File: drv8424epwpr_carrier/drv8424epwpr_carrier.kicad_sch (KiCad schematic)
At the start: 27 parts, among them J1 Input_01x08, J2 Output_01x08, J3 POW_01x02, U1 DRV8424EPWPR, U2 DMP4013LFG-7

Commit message: get ready for PCB
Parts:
- U1: footprint DRV8424EPWPR:HTSSOP28_PWP_TEX -> DRV8424EPWPR:HTSSOP28_PWP_TEX-M
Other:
- note added: "3V3 GND nFAULT nSLEEP AEN APH BEN BPH"
- note added: "AOUT1 AOUT2 VREFA VM GND VREFB BOUT2 BOUT1"
- note added: "VIN GND"
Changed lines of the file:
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@@
+		)
+	)
+	(text "VIN\nGND"
+		(exclude_from_sim no)
+		(at 246.38 45.72 0)
+		(effects
+			(font
+				(size 1.524 1.524)
+			)
+		)
+	)
+	(text "3V3\nGND\nnFAULT\nnSLEEP\nAEN\nAPH\nBEN\nBPH"
+		(exclude_from_sim no)
+		(at 167.132 54.864 0)
+		(effects
+			(font
+				(size 1.524 1.524)
+			)
+		)
+	)
+	(text "AOUT1\nAOUT2\nVREFA\nVM\nGND\nVREFB\nBOUT2\nBOUT1"
+		(exclude_from_sim no)
+		(at 206.502 54.864 0)
+		(effects
+			(font
+				(size 1.524 1.524)
+			)
 		)
 	)
@@
 			)
 		)
-		(property "Footprint" "DRV8424EPWPR:HTSSOP28_PWP_TEX"
+		(property "Footprint" "DRV8424EPWPR:HTSSOP28_PWP_TEX-M"
 			(at 127 100.33 0)
 			(effects

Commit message: update layout
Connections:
- net +3V3: now also J1.8 (Pin_8); no longer J1.1 (Pin_1)
- net AEN: now also J1.2 (Pin_2); no longer J1.5 (Pin_5)
- net APH: now also J1.3 (Pin_3); no longer J1.6 (Pin_6)
- net BEN: now also J1.4 (Pin_4); no longer J1.7 (Pin_7)
- net BOUT1: now also J2.7 (Pin_7); no longer J2.8 (Pin_8)
- net BOUT2: now also J2.8 (Pin_8); no longer J2.7 (Pin_7)
- net BPH: now also J1.5 (Pin_5); no longer J1.8 (Pin_8)
- net GND: now also J1.7 (Pin_7); no longer J1.2 (Pin_2)
- net NFAULT: now also J1.6 (Pin_6); no longer J1.3 (Pin_3)
- net NSLEEP: now also J1.1 (Pin_1); no longer J1.4 (Pin_4)
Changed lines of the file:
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@@
 	(wire
 		(pts
-			(xy 187.96 39.37) (xy 187.96 45.72)
+			(xy 259.08 137.16) (xy 259.08 142.24)
 		)
 		(stroke
@@
 	(wire
 		(pts
-			(xy 259.08 137.16) (xy 259.08 142.24)
+			(xy 93.98 39.37) (xy 105.41 39.37)
 		)
 		(stroke
@@
 	(wire
 		(pts
-			(xy 93.98 39.37) (xy 105.41 39.37)
+			(xy 121.92 118.11) (xy 127 118.11)
 		)
 		(stroke
@@
 	(wire
 		(pts
-			(xy 121.92 118.11) (xy 127 118.11)
+			(xy 114.3 78.74) (xy 124.46 78.74)
 		)
 		(stroke
@@
 	(wire
 		(pts
-			(xy 114.3 78.74) (xy 124.46 78.74)
+			(xy 58.42 109.22) (xy 50.8 109.22)
 		)
 		(stroke
@@
 	(wire
 		(pts
-			(xy 58.42 109.22) (xy 50.8 109.22)
+			(xy 175.26 115.57) (xy 172.72 115.57)
 		)
 		(stroke
@@
 	(wire
 		(pts
-			(xy 175.26 115.57) (xy 172.72 115.57)
+			(xy 68.58 97.79) (xy 72.39 97.79)
 		)
 		(stroke
@@
 	(wire
 		(pts
-			(xy 68.58 97.79) (xy 72.39 97.79)
+			(xy 187.96 60.96) (xy 187.96 66.04)
 		)
 		(stroke
@@
 	(wire
 		(pts
+			(xy 176.53 60.96) (xy 187.96 60.96)
+		)
+		(stroke
+			(width 0)
+			(type default)
+		)
+	)
+	(wire
+		(pts
 			(xy 81.28 73.66) (xy 81.28 78.74)
 		)
@@
 	(wire
 		(pts
-			(xy 187.96 48.26) (xy 187.96 66.04)
-		)
-		(stroke
-			(width 0)
-			(type default)
-		)
-	)
-	(wire
-		(pts
 			(xy 105.41 59.69) (xy 105.41 78.74)
 		)
@@
 	(wire
 		(pts
-			(xy 187.96 45.72) (xy 176.53 45.72)
-		)
-		(stroke
-			(width 0)
-			(type default)
-		)
-	)
-	(wire
-		(pts
 			(xy 259.08 119.38) (xy 259.08 121.92)
 		)
@@
 	(wire
 		(pts
-			(xy 21.59 39.37) (xy 33.02 39.37)
+			(xy 176.53 63.5) (xy 179.07 63.5)
 		)
 		(stroke
@@
 	(wire
 		(pts
-			(xy 74.93 41.91) (xy 74.93 39.37)
+			(xy 21.59 39.37) (xy 33.02 39.37)
 		)
 		(stroke
@@
 	(wire
 		(pts
-			(xy 175.26 118.11) (xy 172.72 118.11)
+			(xy 74.93 41.91) (xy 74.93 39.37)
 		)
 		(stroke
@@
 	(wire
 		(pts
-			(xy 176.53 48.26) (xy 187.96 48.26)
+			(xy 175.26 118.11) (xy 172.72 118.11)
 		)
 		(stroke
@@
 		)
 	)
-	(global_label "BEN"
+	(global_label "BOUT2"
 		(shape input)
-		(at 176.53 60.96 0)
+		(at 215.9 63.5 0)
 		(fields_autoplaced yes)
 		(effects
@@
 		)
 		(property "Intersheetrefs" "${INTERSHEET_REFS}"
-			(at 183.2647 60.96 0)
+			(at 224.9933 63.5 0)
 			(effects
 				(font
@@
 		)
 	)
-	(global_label "BOUT2"
-		(shape input)
-		(at 215.9 60.96 0)
-		(fields_autoplaced yes)
-		(effects
-			(font
-				(size 1.27 1.27)
-			)
-			(justify left)
-		)
-		(property "Intersheetrefs" "${INTERSHEET_REFS}"
-			(at 224.9933 60.96 0)
-			(effects
-				(font
-					(size 1.27 1.27)
-				)
-				(justify left)
-				(hide yes)
-			)
-		)
-	)
 	(global_label "NSLEEP"
 		(shape input)
-		(at 176.53 53.34 0)
+		(at 176.53 45.72 0)
 		(fields_autoplaced yes)
 		(effects
@@
 		)
 		(property "Intersheetrefs" "${INTERSHEET_REFS}"
-			(at 186.6513 53.34 0)
+			(at 186.6513 45.72 0)
 			(effects
 				(font
@@
 		)
 	)
-	(global_label "NFAULT"
+	(global_label "AEN"
 		(shape input)
-		(at 176.53 50.8 0)
+		(at 176.53 48.26 0)
 		(fields_autoplaced yes)
 		(effects
@@
 		)
 		(property "Intersheetrefs" "${INTERSHEET_REFS}"
-			(at 186.3491 50.8 0)
+			(at 183.0833 48.26 0)
 			(effects
 				(font
@@
 	(global_label "APH"
 		(shape input)
+		(at 176.53 50.8 0)
+		(fields_autoplaced yes)
+		(effects
+			(font
+				(size 1.27 1.27)
+			)
+			(justify left)
+		)
+		(property "Intersheetrefs" "${INTERSHEET_REFS}"
+			(at 183.2043 50.8 0)
+			(effects
+				(font
+					(size 1.27 1.27)
+				)
+				(justify left)
+				(hide yes)
+			)
+		)
+	)
+	(global_label "APH"
+		(shape input)
 		(at 175.26 113.03 0)
 		(fields_autoplaced yes)
@@
 		)
 	)
-	(global_label "AEN"
+	(global_label "BEN"
 		(shape input)
-		(at 176.53 55.88 0)
+		(at 176.53 53.34 0)
 		(fields_autoplaced yes)
 		(effects
@@
 		)
 		(property "Intersheetrefs" "${INTERSHEET_REFS}"
-			(at 183.0833 55.88 0)
+			(at 183.2647 53.34 0)
 			(effects
 				(font
@@
 		)
 	)
-	(global_label "VREFA"
+	(global_label "BOUT1"
 		(shape input)
-		(at 172.72 128.27 0)
+		(at 215.9 60.96 0)
 		(fields_autoplaced yes)
 		(effects
@@
 		)
 		(property "Intersheetrefs" "${INTERSHEET_REFS}"
-			(at 181.39 128.27 0)
+			(at 224.9933 60.96 0)
 			(effects
 				(font
@@
 		)
 	)
-	(global_label "VREFA"
+	(global_label "BPH"
 		(shape input)
-		(at 215.9 50.8 0)
+		(at 176.53 55.88 0)
 		(fields_autoplaced yes)
 		(effects
@@
 		)
 		(property "Intersheetrefs" "${INTERSHEET_REFS}"
-			(at 224.57 50.8 0)
+			(at 183.3857 55.88 0)
 			(effects
 				(font
@@
 		)
 	)
-	(global_label "BOUT1"
+	(global_label "VREFA"
 		(shape input)
-		(at 215.9 63.5 0)
+		(at 172.72 128.27 0)
 		(fields_autoplaced yes)
 		(effects
@@
 		)
 		(property "Intersheetrefs" "${INTERSHEET_REFS}"
-			(at 224.9933 63.5 0)
+			(at 181.39 128.27 0)
 			(effects
 				(font
@@
 		)
 	)
-	(global_label "AOUT2"
+	(global_label "NFAULT"
 		(shape input)
-		(at 118.11 113.03 180)
+		(at 176.53 58.42 0)
 		(fields_autoplaced yes)
 		(effects
@@
 				(size 1.27 1.27)
 			)
-			(justify right)
+			(justify left)
 		)
 		(property "Intersheetrefs" "${INTERSHEET_REFS}"
-			(at 109.1981 113.03 0)
+			(at 186.3491 58.42 0)
 			(effects
 				(font
 					(size 1.27 1.27)
 				)
-				(justify right)
+				(justify left)
 				(hide yes)
 			)
 		)
 	)
-	(global_label "BPH"
+	(global_label "VREFA"
 		(shape input)
-		(at 176.53 63.5 0)
+		(at 215.9 50.8 0)
 		(fields_autoplaced yes)
 		(effects
@@
 		)
 		(property "Intersheetrefs" "${INTERSHEET_REFS}"
-			(at 183.3857 63.5 0)
+			(at 224.57 50.8 0)
 			(effects
 				(font
@@
 		)
 	)
-	(global_label "APH"
+	(global_label "AOUT2"
 		(shape input)
-		(at 176.53 58.42 0)
+		(at 118.11 113.03 180)
 		(fields_autoplaced yes)
 		(effects
@@
 				(size 1.27 1.27)
 			)
-			(justify left)
+			(justify right)
 		)
 		(property "Intersheetrefs" "${INTERSHEET_REFS}"
-			(at 183.2043 58.42 0)
+			(at 109.1981 113.03 0)
 			(effects
 				(font
 					(size 1.27 1.27)
 				)
-				(justify left)
+				(justify right)
 				(hide yes)
 			)
@@
 	(symbol
 		(lib_id "power:+3V3")
-		(at 187.96 39.37 0)
+		(at 179.07 63.5 270)
 		(unit 1)
 		(exclude_from_sim no)
@@
 		(on_board yes)
 		(dnp no)
-		(fields_autoplaced yes)
 		(property "Reference" "#PWR013"
-			(at 187.96 43.18 0)
+			(at 175.26 63.5 0)
 			(effects
 				(font
@@
 		)
 		(property "Value" "+3V3"
-			(at 187.96 34.29 0)
+			(at 179.07 65.786 90)
 			(effects
 				(font
 					(size 1.27 1.27)
 				)
+				(justify left)
 			)
 		)
 		(property "Footprint" ""
-			(at 187.96 39.37 0)
+			(at 179.07 63.5 0)
 			(effects
 				(font
@@
 		)
 		(property "Datasheet" ""
-			(at 187.96 39.37 0)
+			(at 179.07 63.5 0)
 			(effects
 				(font
@@
 		)
 		(property "Description" "Power symbol creates a global label with name \"+3V3\""
-			(at 187.96 39.37 0)
+			(at 179.07 63.5 0)
 			(effects
 				(font

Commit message: start routing
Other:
- note added: "I_reg = VREF / 1.32"
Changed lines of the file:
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@@
+		)
+	)
+	(text "I_reg = VREF / 1.32"
+		(exclude_from_sim no)
+		(at 245.618 154.178 0)
+		(effects
+			(font
+				(size 1.27 1.27)
+			)
 		)
 	)

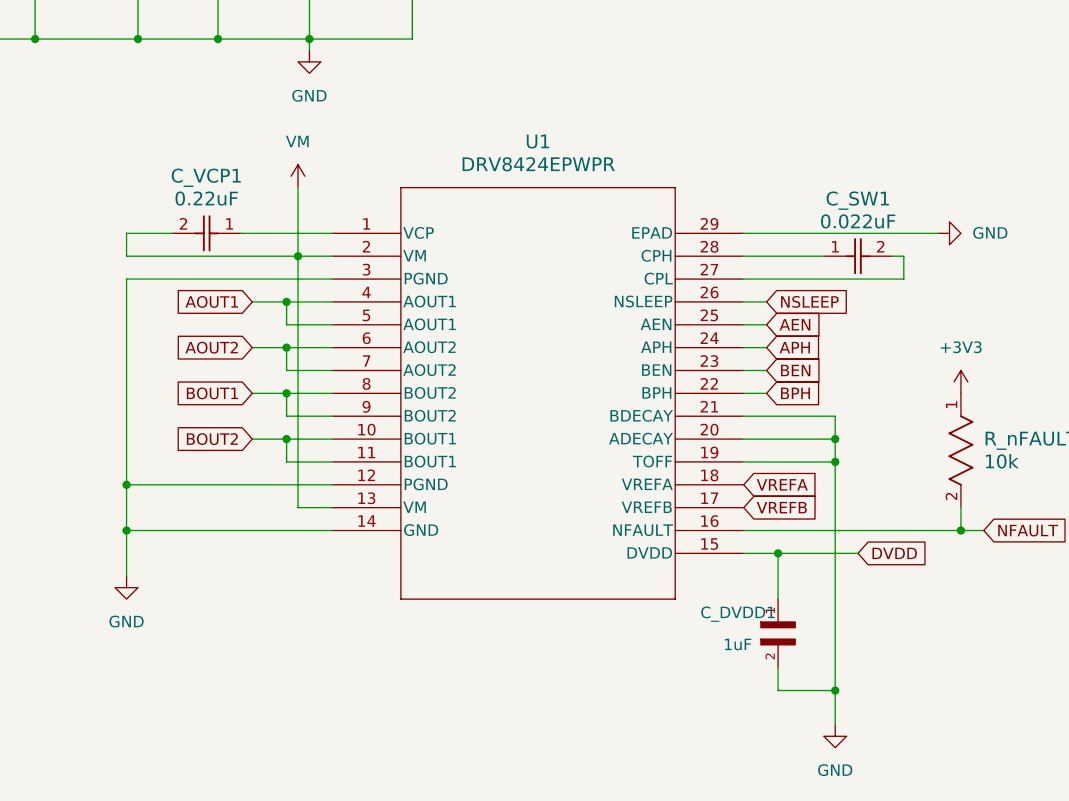
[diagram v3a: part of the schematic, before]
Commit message: update schematic
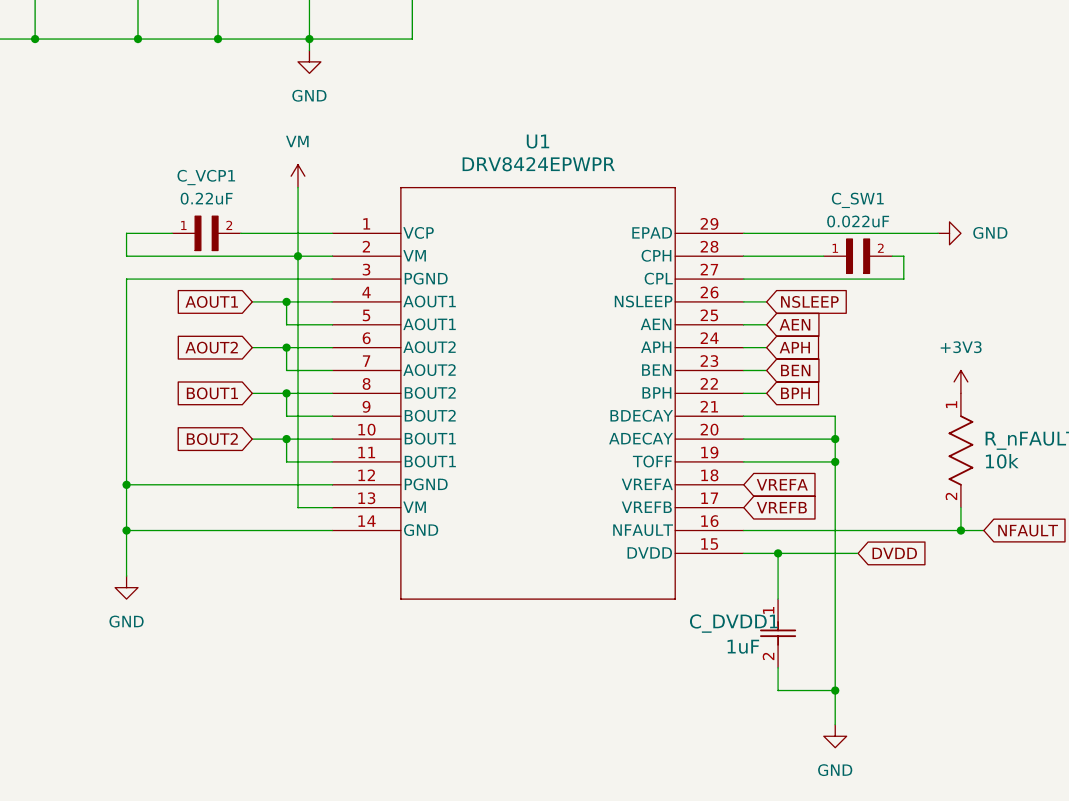
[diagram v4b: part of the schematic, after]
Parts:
- removed C_DVDD1: 1uF, GRM319R71A105KA01D:CAPC3216X95N, symbol GRM319R71A105KA01D:GRM319R71A105KA01D
- removed C_SW1: 0.022uF, C1206C223J8RACTU:CAPC340180_88N_KEM, symbol C1206C223J8RACTU:C1206C223J8RACTU
- removed C_VCP1: 0.22uF, C1206C224K4RACTU:CAPC340180_100N_KEM, symbol C1206C224K4RACTU:C1206C224K4RACTU
- added C_DVDD1: 1uF, Capacitor_SMD:C_0805_2012Metric, symbol C0805C105K8RACTU:C0805C105K8RACTU
- added C_SW1: 0.022uF, Capacitor_SMD:C_0805_2012Metric, symbol C0805C223K8RACTU:C0805C223K8RACTU
- added C_VCP1: 0.22uF, Capacitor_SMD:C_0805_2012Metric, symbol C0805C224K4RACTU:C0805C224K4RACTU
- C_VM1, C_VM2: footprint C0805C103K8RACTU:CAPC220145_88N_KEM -> Capacitor_SMD:C_0805_2012Metric
- LED1: footprint APHCM2012SYCK_F01:LED_APHCM2012SYCK-F01 -> LED_SMD:LED_0805_2012Metric
- LED2, LED4: footprint APHCM2012CGCK_F01:LED_APHCM2012CGCK-F01_KNB -> LED_SMD:LED_0805_2012Metric
- LED3, LED5: footprint APHCM2012SURCK_F01:LED_APHCM2012SURCK-F01 -> LED_SMD:LED_0805_2012Metric
- R1: footprint RC1206FR_07100KL:RC1206N_YAG -> Resistor_SMD:R_1206_3216Metric
- R1_REFA1, R1_REFB1: footprint RC1206FR_0747KL:RC1206N_YAG -> Resistor_SMD:R_1206_3216Metric
- R2, R3, R4: footprint RC1206FR_07590RL:RC1206N_YAG -> Resistor_SMD:R_1206_3216Metric
- R2_REFA1, R2_REFB1: footprint RC1206FR_0716KL:RC1206N_YAG -> Resistor_SMD:R_1206_3216Metric
- R_nFAULT1: footprint RC1206FR_0710KL:RC1206N_YAG -> Resistor_SMD:R_1206_3216Metric
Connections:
- net DVDD: now also C_DVDD1.1
- net GND: now also C_DVDD1.2
- net VM: now also C_VCP1.1
- net at U1.1 (VCP): now also C_VCP1.2
- net at U1.27 (CPL): now also C_SW1.2
- net at U1.28 (CPH): now also C_SW1.1

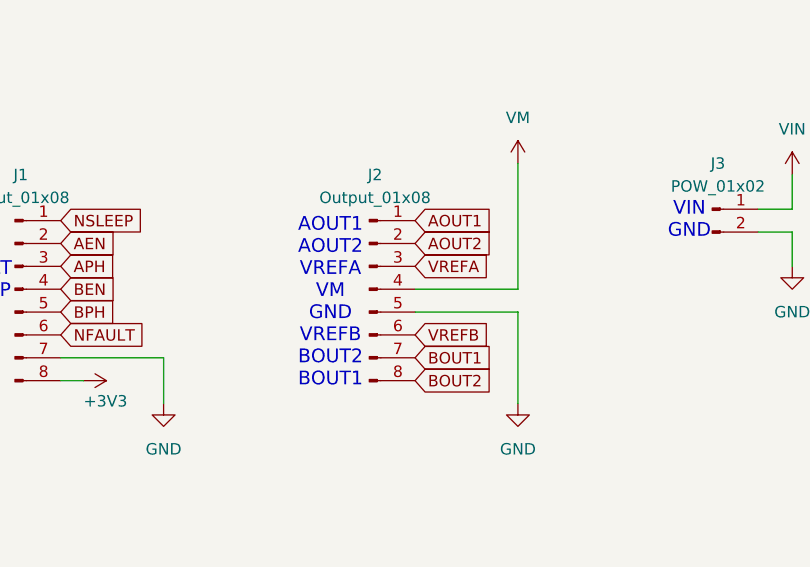
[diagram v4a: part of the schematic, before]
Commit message: update J2 arrange
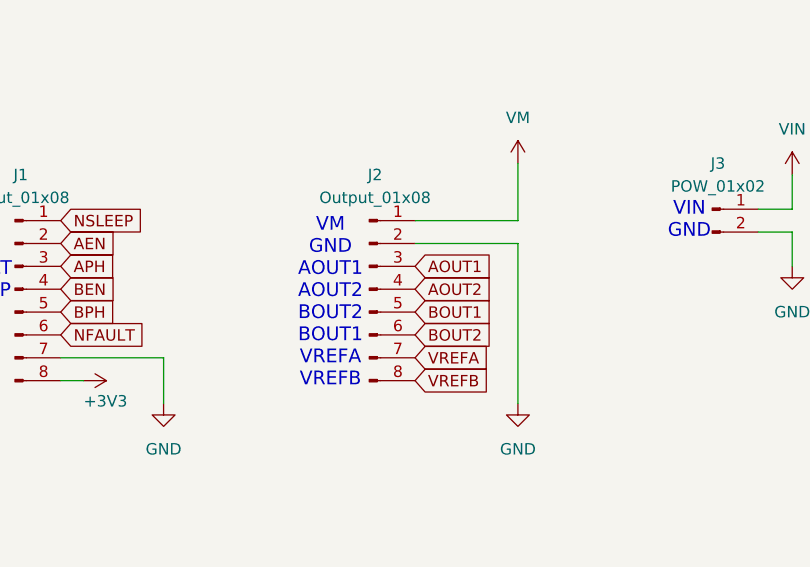
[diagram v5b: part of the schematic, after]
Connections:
- net AOUT1: now also J2.3 (Pin_3); no longer J2.1 (Pin_1)
- net AOUT2: now also J2.4 (Pin_4); no longer J2.2 (Pin_2)
- net BOUT1: now also J2.5 (Pin_5); no longer J2.7 (Pin_7)
- net BOUT2: now also J2.6 (Pin_6); no longer J2.8 (Pin_8)
- net GND: now also J2.2 (Pin_2); no longer J2.5 (Pin_5)
- net VM: now also J2.1 (Pin_1); no longer J2.4 (Pin_4)
- net VREFA: now also J2.7 (Pin_7); no longer J2.3 (Pin_3)
- net VREFB: now also J2.8 (Pin_8); no longer J2.6 (Pin_6)
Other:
- note added: "VM GND AOUT1 AOUT2 BOUT2 BOUT1 VREFA VREFB"
- note removed: "AOUT1 AOUT2 VREFA VM GND VREFB BOUT2 BOUT1"
